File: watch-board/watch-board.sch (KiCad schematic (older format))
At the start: 59 parts

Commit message: Starting Layout -- updated parts with smaller footprints for better layout
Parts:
- removed BT: BAT_ML1220, luke-footprints:BAT_ML1220-F1A, symbol luke:BAT_ML1220
- removed D?: LED_IN-S63AT5UW, Connector_Wire:SolderWire-0.5sqmm_1x02_P4.8mm_D0.9mm_OD2.3mm, symbol luke:LED_IN-S63AT5UW
- removed J: Conn_01x05_Male, Connector_PinHeader_2.54mm:PinHeader_1x05_P2.54mm_Vertical, symbol luke:Conn_01x05_Male
- removed R?: R_604, Resistor_SMD:R_0805_2012Metric, symbol luke:R_604
- added BT1: BAT_ML2020-V1A, luke-footprints:Battery_Panasonic-ML-2020-V1A, symbol luke:BAT_ML2020-V1A
- added D1: LED_WP710A10LSECK-J4, Connector_PinSocket_2.54mm:PinSocket_1x02_P2.54mm_Vertical, symbol luke:LED_WP710A10LSECK-J4
- added J1: Conn_01x05_Male_SMD, Connector_PinHeader_2.54mm:PinHeader_1x05_P2.54mm_Vertical_SMD_Pin1Left, symbol luke:Conn_01x05_Male_SMD
- added R15: R_1.5K, Resistor_SMD:R_0805_2012Metric, symbol luke:R_1.5K
- added R22: R_2.3K, Resistor_SMD:R_0805_2012Metric, symbol luke:R_2.3K
- BZ1: renamed from BZ; footprint Connector_PinSocket_2.54mm:PinSocket_1x02_P2.54mm_Vertical -> Fuse:Fuse_Littelfuse-NANO2-451_453
- Q1, Q2: renamed from Q; footprint digikey-footprints:LED_2-SMD_No_Lead_1.7x0.8mm -> Digikey-footprints:LED_2-SMD_No_Lead_1.7x0.8mm
- gave numbers to parts that had none: 6
- renumbered C to C1, C to C10, C to C11, C to C12, C to C13, C to C14, C to C15, C to C16, C to C17, C to C18, C to C19, C to C2, C to C3, C to C4, C to C5, C to C6, C to C7, C to C8, C to C9, DS to DS1, DS to DS2, L to L1, L to L2, R to R1, R to R10, R to R11, R to R12, R to R16, R to R17, R to R19, R to R2, R to R21, R to R3, R to R4, R to R5, R to R6, R to R7, R to R8, R to R9, S to S1, SC to SC1, U to U1, U to U2, U to U3, U to U4, XTAL to XTAL1
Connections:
- net GND: now also BT1.Neg (-), D1.1 (K), J1.4 (Pin_4), R22.2
- net LIGHT: now also R15.1
- net RST: now also J1.1 (Pin_1)
- net SWCLK: now also J1.2 (Pin_2)
- net SWDIO: now also J1.3 (Pin_3)
- net VDD: now also J1.5 (Pin_5)
- net at U2.14 (VBAT): now also BT1.Pos (+)
- new net: D1.2 (A), R15.2, R22.1

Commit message: Layout (Rev 1) Complete
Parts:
- removed J1: Conn_01x05_Male_SMD, Connector_PinHeader_2.54mm:PinHeader_1x05_P2.54mm_Vertical_SMD_Pin1Left, symbol luke:Conn_01x05_Male_SMD
- added J1, J2, J3, J4, J5: Conn_PAD, luke-footprints:Connector_PAD_1mm_Circ, symbol luke:Conn_PAD
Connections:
- net VCC is gone; now on net VDD: R11.1, R12.1, R20.1
- net GND: now also J4.1
- net RST: now also J1.1
- net SWCLK: now also J2.1
- net SWDIO: now also J3.1
- net VDD: now also J5.1
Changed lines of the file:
@@
 NoConn ~ 8950 2700
 NoConn ~ 8950 2800
-Text Label 8100 4500 0    50   ~ 0
+Text Label 8050 4400 0    50   ~ 0
 RST
-Text Label 8100 4600 0    50   ~ 0
+Text Label 8050 4500 0    50   ~ 0
 SWCLK
-Text Label 8100 4700 0    50   ~ 0
+Text Label 8050 4600 0    50   ~ 0
 SWDIO
 $Comp
 L power:GND #PWR032
 U 1 1 5ED60068
-P 8100 4800
-F 0 "#PWR032" H 8100 4550 50  0001 C CNN
-F 1 "GND" V 8105 4672 50  0000 R CNN
-F 2 "" H 8100 4800 50  0001 C CNN
-F 3 "" H 8100 4800 50  0001 C CNN
-	1    8100 4800
+P 8050 4700
+F 0 "#PWR032" H 8050 4450 50  0001 C CNN
+F 1 "GND" V 8055 4572 50  0000 R CNN
+F 2 "" H 8050 4700 50  0001 C CNN
+F 3 "" H 8050 4700 50  0001 C CNN
+	1    8050 4700
 	0    -1   -1   0
 $EndComp
@@
 L power:VDD #PWR033
 U 1 1 5ED5B97B
-P 8100 4900
-F 0 "#PWR033" H 8100 4750 50  0001 C CNN
-F 1 "VDD" V 8117 5028 50  0000 L CNN
-F 2 "" H 8100 4900 50  0001 C CNN
-F 3 "" H 8100 4900 50  0001 C CNN
-	1    8100 4900
+P 8050 4800
+F 0 "#PWR033" H 8050 4650 50  0001 C CNN
+F 1 "VDD" V 8067 4928 50  0000 L CNN
+F 2 "" H 8050 4800 50  0001 C CNN
+F 3 "" H 8050 4800 50  0001 C CNN
+	1    8050 4800
 	0    1    1    0
 $EndComp
@@
 Wire Wire Line
 	4850 2350 4850 2300
-$Comp
-L power:VCC #PWR014
-U 1 1 5FB6C587
-P 5050 2250
-F 0 "#PWR014" H 5050 2100 50  0001 C CNN
-F 1 "VCC" H 5065 2423 50  0000 C CNN
-F 2 "" H 5050 2250 50  0001 C CNN
-F 3 "" H 5050 2250 50  0001 C CNN
-	1    5050 2250
-	1    0    0    -1
-$EndComp
 Wire Wire Line
 	4850 2700 4850 2650
@@
 $EndComp
 $Comp
-L power:VCC #PWR035
-U 1 1 5F7E6088
-P 12000 950
-F 0 "#PWR035" H 12000 800 50  0001 C CNN
-F 1 "VCC" H 12015 1123 50  0000 C CNN
-F 2 "" H 12000 950 50  0001 C CNN
-F 3 "" H 12000 950 50  0001 C CNN
-	1    12000 950
-	1    0    0    -1
-$EndComp
-$Comp
 L power:GND #PWR036
 U 1 1 5F7E6997
@@
 	-1   0    0    1
 $EndComp
-$Comp
-L luke:Conn_01x05_Male_SMD J1
-U 1 1 5F7820CD
-P 7900 4700
-F 0 "J1" H 8000 5200 50  0000 C CNN
-F 1 "Conn_01x05_Male_SMD" H 8000 5100 50  0000 C CNN
-F 2 "Connector_PinHeader_2.54mm:PinHeader_1x05_P2.54mm_Vertical_SMD_Pin1Left" H 7900 4300 50  0001 C CNN
-F 3 "https://www.molex.com/pdm_docs/sd/878980524_sd.pdf" H 7900 4700 50  0001 C CNN
-F 4 "https://www.digikey.com/product-detail/en/molex/0878980524/WM14825-ND/3264904" H 7900 4700 50  0001 C CNN "Purchasing Link"
-	1    7900 4700
-	1    0    0    -1
-$EndComp
 Wire Notes Line
 	8000 4050 8500 4050
 Wire Notes Line
 	7500 5050 8500 5050
+$Comp
+L power:VDD #PWR035
+U 1 1 5F4A49CD
+P 12000 950
+F 0 "#PWR035" H 12000 800 50  0001 C CNN
+F 1 "VDD" H 12015 1123 50  0000 C CNN
+F 2 "" H 12000 950 50  0001 C CNN
+F 3 "" H 12000 950 50  0001 C CNN
+	1    12000 950
+	1    0    0    -1
+$EndComp
+$Comp
+L power:VDD #PWR014
+U 1 1 5F4A50B9
+P 5050 2250
+F 0 "#PWR014" H 5050 2100 50  0001 C CNN
+F 1 "VDD" H 5065 2423 50  0000 C CNN
+F 2 "" H 5050 2250 50  0001 C CNN
+F 3 "" H 5050 2250 50  0001 C CNN
+	1    5050 2250
+	1    0    0    -1
+$EndComp
+$Comp
+L luke:Conn_PAD J1
+U 1 1 5F4F53E0
+P 7850 4400
+F 0 "J1" H 7800 4400 50  0000 C CNN
+F 1 "Conn_PAD" H 8400 4850 50  0001 C CNN
+F 2 "luke-footprints:Connector_PAD_1mm_Circ" H 7850 4050 50  0001 C CNN
+F 3 "~" H 7850 4450 50  0001 C CNN
+	1    7850 4400
+	1    0    0    -1
+$EndComp
+$Comp
+L luke:Conn_PAD J2
+U 1 1 5F4F6177
+P 7850 4500
+F 0 "J2" H 7800 4500 50  0000 C CNN
+F 1 "Conn_PAD" H 8400 4950 50  0001 C CNN
+F 2 "luke-footprints:Connector_PAD_1mm_Circ" H 7850 4150 50  0001 C CNN
+F 3 "~" H 7850 4550 50  0001 C CNN
+	1    7850 4500
+	1    0    0    -1
+$EndComp
+$Comp
+L luke:Conn_PAD J4
+U 1 1 5F4F83BC
+P 7850 4700
+F 0 "J4" H 7800 4700 50  0000 C CNN
+F 1 "Conn_PAD" H 8400 5150 50  0001 C CNN
+F 2 "luke-footprints:Connector_PAD_1mm_Circ" H 7850 4350 50  0001 C CNN
+F 3 "~" H 7850 4750 50  0001 C CNN
+	1    7850 4700
+	1    0    0    -1
+$EndComp
+$Comp
+L luke:Conn_PAD J3
+U 1 1 5F5027C3
+P 7850 4600
+F 0 "J3" H 7800 4600 50  0000 C CNN
+F 1 "Conn_PAD" H 8400 5050 50  0001 C CNN
+F 2 "luke-footprints:Connector_PAD_1mm_Circ" H 7850 4250 50  0001 C CNN
+F 3 "~" H 7850 4650 50  0001 C CNN
+	1    7850 4600
+	1    0    0    -1
+$EndComp
+$Comp
+L luke:Conn_PAD J5
+U 1 1 5F50E150
+P 7850 4800
+F 0 "J5" H 7800 4800 50  0000 C CNN
+F 1 "Conn_PAD" H 8400 5250 50  0001 C CNN
+F 2 "luke-footprints:Connector_PAD_1mm_Circ" H 7850 4450 50  0001 C CNN
+F 3 "~" H 7850 4850 50  0001 C CNN
+	1    7850 4800
+	1    0    0    -1
+$EndComp
 $EndSCHEMATC

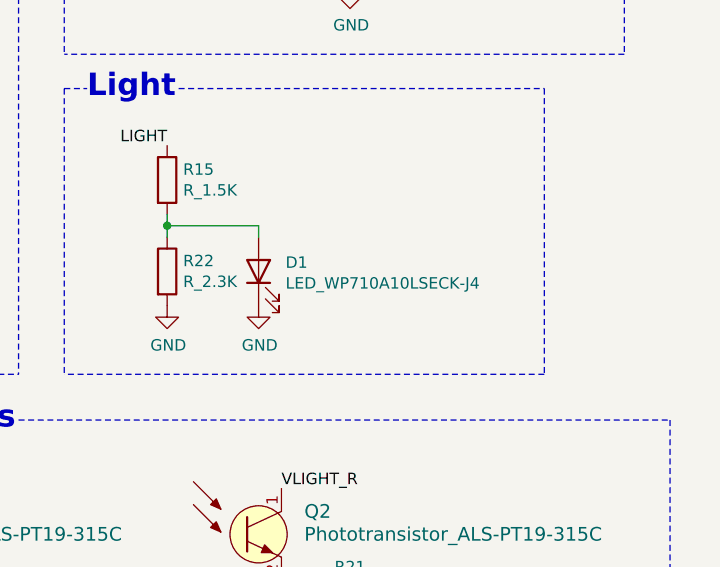
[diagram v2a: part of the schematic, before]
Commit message: starting layout. connected LCDs
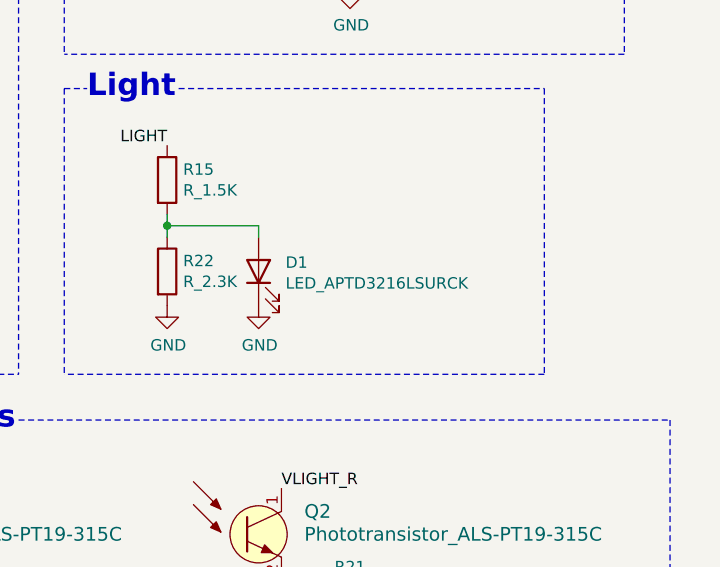
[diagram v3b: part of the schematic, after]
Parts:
- removed D1: LED_WP710A10LSECK-J4, Connector_PinSocket_2.54mm:PinSocket_1x02_P2.54mm_Vertical, symbol luke:LED_WP710A10LSECK-J4
- added D1: LED_APTD3216LSURCK, LED_SMD:LED_1206_3216Metric, symbol luke:LED_APTD3216LSURCK
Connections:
- net GND: now also D1.1 (K)
- net at R15.2, R22.1: now also D1.2 (A)
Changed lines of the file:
@@
 	1    0    0    -1
-$EndComp
-$Comp
-L luke:LED_WP710A10LSECK-J4 D1
-U 1 1 5F51AD34
-P 11600 3400
-F 0 "D1" V 11639 3282 50  0000 R CNN
-F 1 "LED_WP710A10LSECK-J4" V 11548 3282 50  0000 R CNN
-F 2 "Connector_PinSocket_2.54mm:PinSocket_1x02_P2.54mm_Vertical" H 11600 3400 50  0001 C CNN
-F 3 "https://www.kingbrightusa.com/images/catalog/SPEC/WP710A10LSECK-J4.pdf" H 11600 3400 50  0001 C CNN
-F 4 "https://www.digikey.com/product-detail/en/kingbright/WP710A10LSECK-J4/754-1912-ND/5177413" H 11600 3400 50  0001 C CNN "Purchasing Link"
-F 5 "754-1912-ND" H 11600 3400 50  0001 C CNN "Digi-Key_PN"
-	1    11600 3400
-	0    -1   -1   0
 $EndComp
 Wire Wire Line
@@
 	1    0    0    -1
 $EndComp
+$Comp
+L luke:LED_APTD3216LSURCK D1
+U 1 1 5F49ED87
+P 11600 3400
+F 0 "D1" V 11639 3282 50  0000 R CNN
+F 1 "LED_APTD3216LSURCK" V 11548 3282 50  0000 R CNN
+F 2 "LED_SMD:LED_1206_3216Metric" H 11600 3400 50  0001 C CNN
+F 3 "https://www.kingbrightusa.com/images/catalog/SPEC/APTD3216LQBC-D.pdf" H 11600 3400 50  0001 C CNN
+F 4 "https://www.digikey.com/product-detail/en/kingbright/APTD3216LSURCK/754-2050-6-ND/7043124" H 11600 3400 50  0001 C CNN "Purchasing Link"
+F 5 "754-2050-6-ND" H 11600 3400 50  0001 C CNN "Digi-Key_PN"
+	1    11600 3400
+	0    -1   -1   0
+$EndComp
 $EndSCHEMATC

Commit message: all wiring done except gnd
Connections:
- net GND: now also C3.2, C4.2
- net LIGHT_L: now also U4.11 (PA5); no longer U4.8 (PA2)
- net LIGHT_R: now also U4.8 (PA2); no longer U4.9 (PA3)
- net VDD: now also U1.2 (VLCD), U1.3 (VDD)
- net VLIGHT_L: now also U4.12 (PA6); no longer U4.11 (PA5)
- net VLIGHT_R: now also U4.9 (PA3); no longer U4.12 (PA6)
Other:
- note added: "C3: Place near Pin 2\nC4: Place near Pin 3"
- moved on the sheet: C3, C4
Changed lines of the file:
@@
 	1    0    0    -1
 $EndComp
-Connection ~ 3600 1450
-Wire Wire Line
-	3800 1450 3600 1450
-Wire Wire Line
-	3800 1500 3800 1450
-Wire Wire Line
-	3600 1450 3600 1400
-Wire Wire Line
-	3400 1450 3600 1450
-Wire Wire Line
-	3400 1500 3400 1450
+Connection ~ 4900 1050
+Wire Wire Line
+	5100 1050 4900 1050
+Wire Wire Line
+	5100 1100 5100 1050
+Wire Wire Line
+	4900 1050 4900 1000
+Wire Wire Line
+	4700 1050 4900 1050
+Wire Wire Line
+	4700 1100 4700 1050
 Text Label 2900 2650 2    50   ~ 0
 1A
@@
 L luke:C_0.1uF C4
 U 1 1 5F2B40B8
-P 3800 1700
-F 0 "C4" H 3915 1796 50  0000 L CNN
-F 1 "C_0.1uF" H 3915 1705 50  0000 L CNN
-F 2 "Capacitor_SMD:C_0805_2012Metric" H 3838 2300 50  0001 C CNN
-F 3 "https://api.kemet.com/component-edge/download/datasheet/C0805C104M3RACTU.pdf" H 3825 2550 50  0001 C CNN
-F 4 "https://www.digikey.com/product-detail/en/kemet/C0805C104M3RACTU/399-8000-1-ND/3471723" H 4225 2200 60  0001 C CNN "Purchasing Link"
-F 5 "399-8000-1-ND" H 3800 2400 50  0001 C CNN "Digi-Key_PN"
-	1    3800 1700
+P 5100 1300
+F 0 "C4" H 5215 1396 50  0000 L CNN
+F 1 "C_0.1uF" H 5215 1305 50  0000 L CNN
+F 2 "Capacitor_SMD:C_0805_2012Metric" H 5138 1900 50  0001 C CNN
+F 3 "https://api.kemet.com/component-edge/download/datasheet/C0805C104M3RACTU.pdf" H 5125 2150 50  0001 C CNN
+F 4 "https://www.digikey.com/product-detail/en/kemet/C0805C104M3RACTU/399-8000-1-ND/3471723" H 5525 1800 60  0001 C CNN "Purchasing Link"
+F 5 "399-8000-1-ND" H 5100 2000 50  0001 C CNN "Digi-Key_PN"
+	1    5100 1300
 	1    0    0    -1
 $EndComp
@@
 L luke:C_0.1uF C3
 U 1 1 5F2B2087
-P 3400 1700
-F 0 "C3" H 3300 1800 50  0000 R CNN
-F 1 "C_0.1uF" H 3300 1700 50  0000 R CNN
-F 2 "Capacitor_SMD:C_0805_2012Metric" H 3438 2300 50  0001 C CNN
-F 3 "https://api.kemet.com/component-edge/download/datasheet/C0805C104M3RACTU.pdf" H 3425 2550 50  0001 C CNN
-F 4 "https://www.digikey.com/product-detail/en/kemet/C0805C104M3RACTU/399-8000-1-ND/3471723" H 3825 2200 60  0001 C CNN "Purchasing Link"
-F 5 "399-8000-1-ND" H 3400 2400 50  0001 C CNN "Digi-Key_PN"
-	1    3400 1700
+P 4700 1300
+F 0 "C3" H 4600 1400 50  0000 R CNN
+F 1 "C_0.1uF" H 4600 1300 50  0000 R CNN
+F 2 "Capacitor_SMD:C_0805_2012Metric" H 4738 1900 50  0001 C CNN
+F 3 "https://api.kemet.com/component-edge/download/datasheet/C0805C104M3RACTU.pdf" H 4725 2150 50  0001 C CNN
+F 4 "https://www.digikey.com/product-detail/en/kemet/C0805C104M3RACTU/399-8000-1-ND/3471723" H 5125 1800 60  0001 C CNN "Purchasing Link"
+F 5 "399-8000-1-ND" H 4700 2000 50  0001 C CNN "Digi-Key_PN"
+	1    4700 1300
 	1    0    0    -1
 $EndComp
@@
 L power:VDD #PWR07
 U 1 1 5F4E8A36
-P 3600 1400
-F 0 "#PWR07" H 3600 1250 50  0001 C CNN
-F 1 "VDD" H 3615 1573 50  0000 C CNN
-F 2 "" H 3600 1400 50  0001 C CNN
-F 3 "" H 3600 1400 50  0001 C CNN
-	1    3600 1400
+P 4900 1000
+F 0 "#PWR07" H 4900 850 50  0001 C CNN
+F 1 "VDD" H 4915 1173 50  0000 C CNN
+F 2 "" H 4900 1000 50  0001 C CNN
+F 3 "" H 4900 1000 50  0001 C CNN
+	1    4900 1000
 	1    0    0    -1
 $EndComp
@@
 	1    0    0    -1
 $EndComp
+Text Label 10050 2000 0    50   ~ 0
+LIGHT_L
 Text Label 10050 1700 0    50   ~ 0
-LIGHT_L
-Text Label 10050 1800 0    50   ~ 0
 LIGHT_R
 Text Label 10200 4900 0    50   ~ 0
@@
 Text Label 9600 4350 0    50   ~ 0
 VLIGHT_L
+Text Label 10050 1800 0    50   ~ 0
+VLIGHT_R
 Text Label 10050 2100 0    50   ~ 0
-VLIGHT_R
-Text Label 10050 2000 0    50   ~ 0
 VLIGHT_L
 Text Label 10050 2200 0    50   ~ 0
@@
 	0    -1   -1   0
 $EndComp
+Wire Wire Line
+	5100 1400 5100 1450
+Wire Wire Line
+	5100 1450 4900 1450
+Wire Wire Line
+	4700 1450 4700 1400
+Wire Wire Line
+	4900 1450 4900 1500
+Connection ~ 4900 1450
+Wire Wire Line
+	4900 1450 4700 1450
+$Comp
+L power:GND #PWR041
+U 1 1 5F581391
+P 4900 1500
+F 0 "#PWR041" H 4900 1250 50  0001 C CNN
+F 1 "GND" H 4905 1327 50  0000 C CNN
+F 2 "" H 4900 1500 50  0001 C CNN
+F 3 "" H 4900 1500 50  0001 C CNN
+	1    4900 1500
+	1    0    0    -1
+$EndComp
+$Comp
+L power:VDD #PWR040
+U 1 1 5F585EBB
+P 3800 1800
+F 0 "#PWR040" H 3800 1650 50  0001 C CNN
+F 1 "VDD" H 3815 1973 50  0000 C CNN
+F 2 "" H 3800 1800 50  0001 C CNN
+F 3 "" H 3800 1800 50  0001 C CNN
+	1    3800 1800
+	1    0    0    -1
+$EndComp
+$Comp
+L power:VDD #PWR039
+U 1 1 5F58699A
+P 3400 1800
+F 0 "#PWR039" H 3400 1650 50  0001 C CNN
+F 1 "VDD" H 3415 1973 50  0000 C CNN
+F 2 "" H 3400 1800 50  0001 C CNN
+F 3 "" H 3400 1800 50  0001 C CNN
+	1    3400 1800
+	1    0    0    -1
+$EndComp
+Text Notes 3800 1050 0    50   ~ 0
+C3: Place near Pin 2\nC4: Place near Pin 3
 $EndSCHEMATC

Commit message: finished wiring
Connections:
- net COM1: no longer U1.32 (COM2)
- net COM2: no longer U1.31 (COM1)
- no-connect marks 17 -> 19
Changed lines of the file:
@@
 Connection ~ 4350 2950
 Wire Wire Line
-	4550 2950 4550 3050
-Wire Wire Line
-	4350 2950 4550 2950
+	4650 2950 4650 3050
 Wire Wire Line
 	4350 3000 4300 3000
@@
 L power:GND #PWR010
 U 1 1 5FA072DD
-P 4550 3050
-F 0 "#PWR010" H 4550 2800 50  0001 C CNN
-F 1 "GND" H 4555 2877 50  0000 C CNN
-F 2 "" H 4550 3050 50  0001 C CNN
-F 3 "" H 4550 3050 50  0001 C CNN
-	1    4550 3050
-	1    0    0    -1
-$EndComp
-Connection ~ 4350 3500
-Wire Wire Line
-	4350 3500 4450 3500
-Connection ~ 4400 3400
-Wire Wire Line
-	4400 3400 4450 3400
-Text Label 4450 3400 0    50   ~ 0
+P 4650 3050
+F 0 "#PWR010" H 4650 2800 50  0001 C CNN
+F 1 "GND" H 4655 2877 50  0000 C CNN
+F 2 "" H 4650 3050 50  0001 C CNN
+F 3 "" H 4650 3050 50  0001 C CNN
+	1    4650 3050
+	1    0    0    -1
+$EndComp
+Text Label 4300 3200 0    50   ~ 0
 COM2
-Text Label 4450 3500 0    50   ~ 0
+Text Label 4300 3500 0    50   ~ 0
 COM1
-Wire Wire Line
-	4400 3200 4300 3200
-Wire Wire Line
-	4400 3400 4400 3200
-Wire Wire Line
-	4300 3400 4400 3400
-Wire Wire Line
-	4350 3300 4300 3300
-Wire Wire Line
-	4350 3500 4350 3300
-Wire Wire Line
-	4300 3500 4350 3500
 NoConn ~ 4300 2300
 Wire Wire Line
@@
 NoConn ~ 2900 3650
 NoConn ~ 2900 3550
-$Comp
-L luke:Display-Driver_PCA8561ANH U1
-U 1 1 5F8BB753
-P 3600 3800
-F 0 "U1" H 4400 3700 50  0000 C CNN
-F 1 "Display-Driver_PCA8561ANH" H 4400 3600 50  0000 C CNN
-F 2 "Package_DFN_QFN:QFN-32-1EP_5x5mm_P0.5mm_EP3.6x3.6mm" H 3600 1600 50  0001 C CNN
-F 3 "https://www.nxp.com/docs/en/data-sheet/PCA8561.pdf" H 4200 5500 50  0001 C CNN
-F 4 "568-13032-1-ND" H 3600 1900 50  0001 C CNN "Digi-Key_PN"
-F 5 "https://www.digikey.com/product-detail/en/nxp-usa-inc/PCA8561AHN-AY/568-13032-1-ND/6137585" H 3550 1750 50  0001 C CNN "Purchasing Link"
-	1    3600 3800
-	1    0    0    -1
-$EndComp
 Connection ~ 4900 1050
 Wire Wire Line
@@
 Text Notes 3800 1050 0    50   ~ 0
 C3: Place near Pin 2\nC4: Place near Pin 3
+NoConn ~ 4300 3300
+$Comp
+L luke:Display-Driver_PCA8561ANH U1
+U 1 1 5F8BB753
+P 3600 3800
+F 0 "U1" H 4400 3700 50  0000 C CNN
+F 1 "Display-Driver_PCA8561ANH" H 4400 3600 50  0000 C CNN
+F 2 "Package_DFN_QFN:QFN-32-1EP_5x5mm_P0.5mm_EP3.6x3.6mm" H 3600 1600 50  0001 C CNN
+F 3 "https://www.nxp.com/docs/en/data-sheet/PCA8561.pdf" H 4200 5500 50  0001 C CNN
+F 4 "568-13032-1-ND" H 3600 1900 50  0001 C CNN "Digi-Key_PN"
+F 5 "https://www.digikey.com/product-detail/en/nxp-usa-inc/PCA8561AHN-AY/568-13032-1-ND/6137585" H 3550 1750 50  0001 C CNN "Purchasing Link"
+	1    3600 3800
+	1    0    0    -1
+$EndComp
+Wire Wire Line
+	4350 2950 4650 2950
+NoConn ~ 4300 3400
 $EndSCHEMATC
